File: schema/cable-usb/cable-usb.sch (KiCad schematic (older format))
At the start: 2 parts

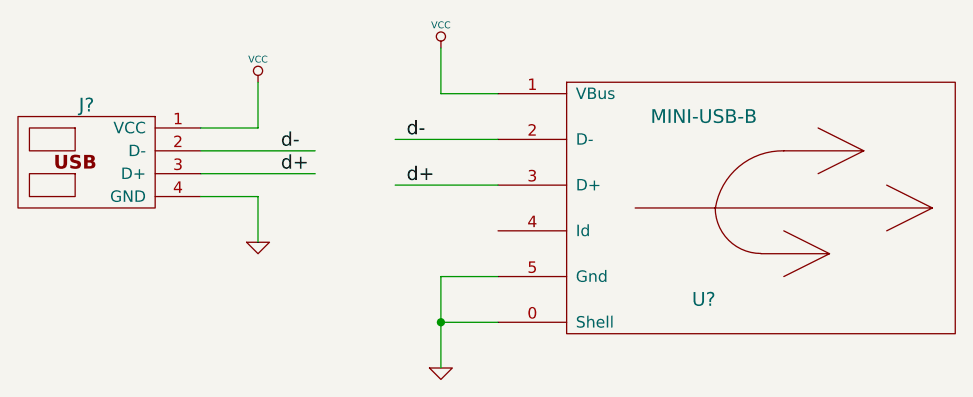
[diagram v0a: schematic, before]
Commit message: Annotation is performed on cable schemas.
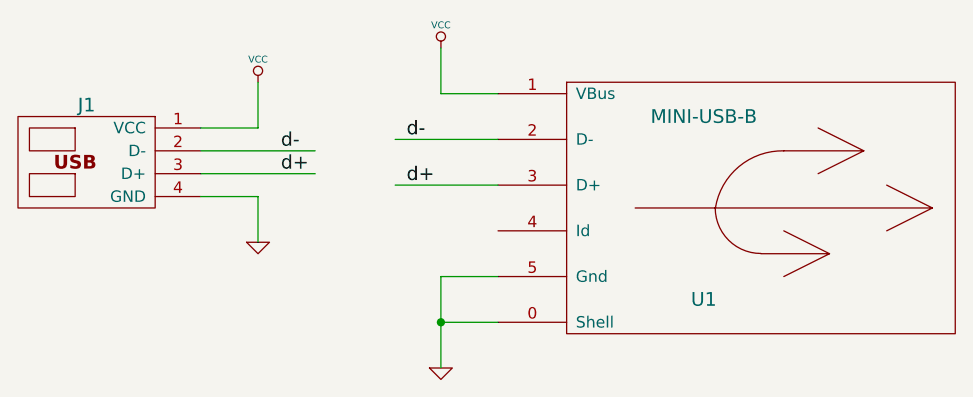
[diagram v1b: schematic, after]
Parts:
- gave numbers to parts that had none: 2
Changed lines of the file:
@@
-EESchema Schematic File Version 2  date Mon 27 Aug 2012 04:51:01 PM MSK
+EESchema Schematic File Version 2  date Wed 05 Sep 2012 02:15:31 PM MSK
 LIBS:power
 LIBS:device
@@
 LIBS:my_comps
 LIBS:con-usb
-EELAYER 43  0
+LIBS:cable-usb-cache
+EELAYER 25  0
 EELAYER END
 $Descr A4 11700 8267
@@
 Sheet 1 1
 Title ""
-Date "27 aug 2012"
+Date "5 sep 2012"
 Rev ""
 Comp ""
@@
 	6250 3850 5800 3850
 $Comp
-L GND #PWR?
+L GND #PWR4
 U 1 1 503B6B7B
 P 6000 4850
-F 0 "#PWR?" H 6000 4850 30  0001 C CNN
+F 0 "#PWR4" H 6000 4850 30  0001 C CNN
 F 1 "GND" H 6000 4780 30  0001 C CNN
 	1    6000 4850
@@
 $EndComp
 $Comp
-L VCC #PWR?
+L VCC #PWR3
 U 1 1 503B6B56
 P 6000 3450
-F 0 "#PWR?" H 6000 3550 30  0001 C CNN
+F 0 "#PWR3" H 6000 3550 30  0001 C CNN
 F 1 "VCC" H 6000 3550 30  0000 C CNN
 	1    6000 3450
@@
 d-
 $Comp
-L VCC #PWR?
+L VCC #PWR1
 U 1 1 503B6B3F
 P 5200 3600
-F 0 "#PWR?" H 5200 3700 30  0001 C CNN
+F 0 "#PWR1" H 5200 3700 30  0001 C CNN
 F 1 "VCC" H 5200 3700 30  0000 C CNN
 	1    5200 3600
@@
 $EndComp
 $Comp
-L GND #PWR?
+L GND #PWR2
 U 1 1 503B6B39
 P 5200 4300
-F 0 "#PWR?" H 5200 4300 30  0001 C CNN
+F 0 "#PWR2" H 5200 4300 30  0001 C CNN
 F 1 "GND" H 5200 4230 30  0001 C CNN
 	1    5200 4300
@@
 $EndComp
 $Comp
-L USB_2_VALID J?
+L USB_2_VALID J1
 U 1 1 503B6AF6
 P 4750 3950
-F 0 "J?" H 5050 4200 60  0000 C CNN
+F 0 "J1" H 5050 4200 60  0000 C CNN
 F 1 "USB_2_VALID" H 5050 3650 60  0001 C CNN
 F 4 "VCC" H 4425 4100 50  0001 C CNN "VCC"
@@
 $EndComp
 $Comp
-L MINI-USB-B U?
+L MINI-USB-B U1
 U 1 1 503B6A0B
 P 7150 4150
-F 0 "U?" H 7150 3750 60  0000 C CNN
+F 0 "U1" H 7150 3750 60  0000 C CNN
 F 1 "MINI-USB-B" H 7150 4550 60  0000 C CNN
 	1    7150 4150
